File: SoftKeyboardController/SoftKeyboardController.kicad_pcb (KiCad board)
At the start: 2 copper layers, 175.9 x 135.9 mm, 44 parts, among them IC1 PCA9956BTWY, J1 Barrel_Jack, J2 Conn_01x08_Socket, J3 Motor 1, J4 Motor 2, J5 Conn_01x12_Socket, J6 Conn_01x12_Socket, J7 EXT IMU Connection, J8 Conn_01x08_Socket, Q1 Q_NMOS_GDS, Q10 Q_NMOS_GDS, Q11 Q_NMOS_GDS, Q12 Q_NMOS_GDS, Q13 Q_NMOS_GDS, Q14 Q_NMOS_GDS, Q15 Q_NMOS_GDS, Q16 Q_NMOS_GDS, Q2 Q_NMOS_GDS, Q3 Q_NMOS_GDS, Q4 Q_NMOS_GDS, Q5 Q_NMOS_GDS, Q6 Q_NMOS_GDS, Q7 Q_NMOS_GDS, Q8 Q_NMOS_GDS, Q9 Q_NMOS_GDS, U1 Motor Driver DRV8847PWR, U2 ADC128D818, U3 ADC128D818, U4 PI4IOE5V9539LEX

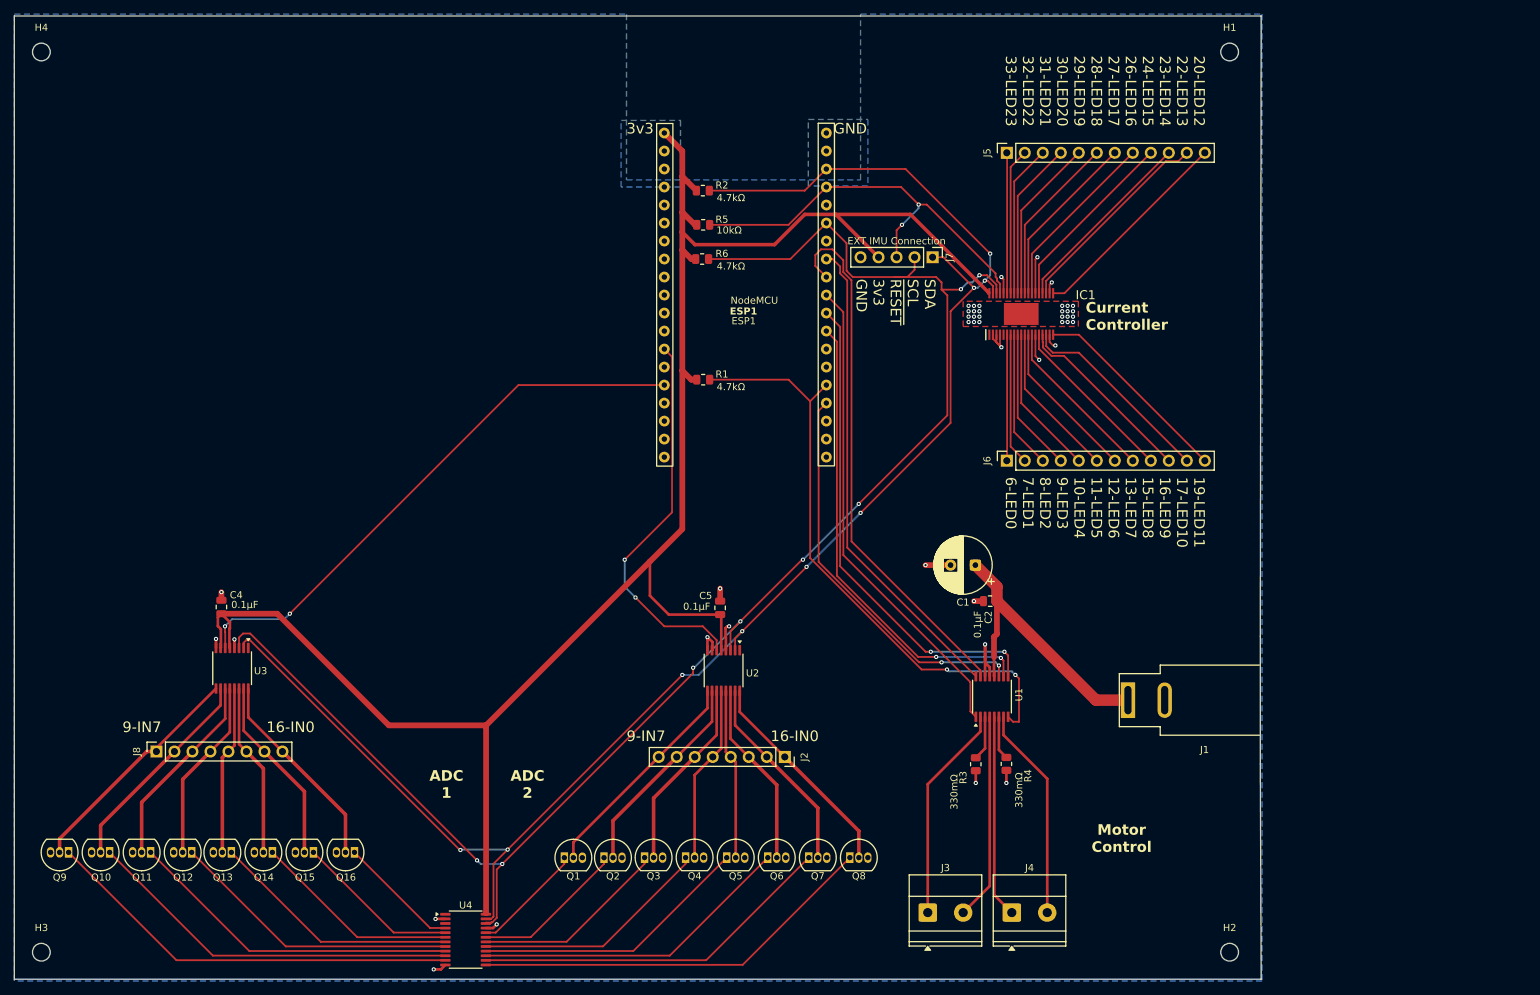
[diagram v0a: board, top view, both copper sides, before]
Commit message: Shrink Footprint
Relocated and re-traced board to improve overall footprint
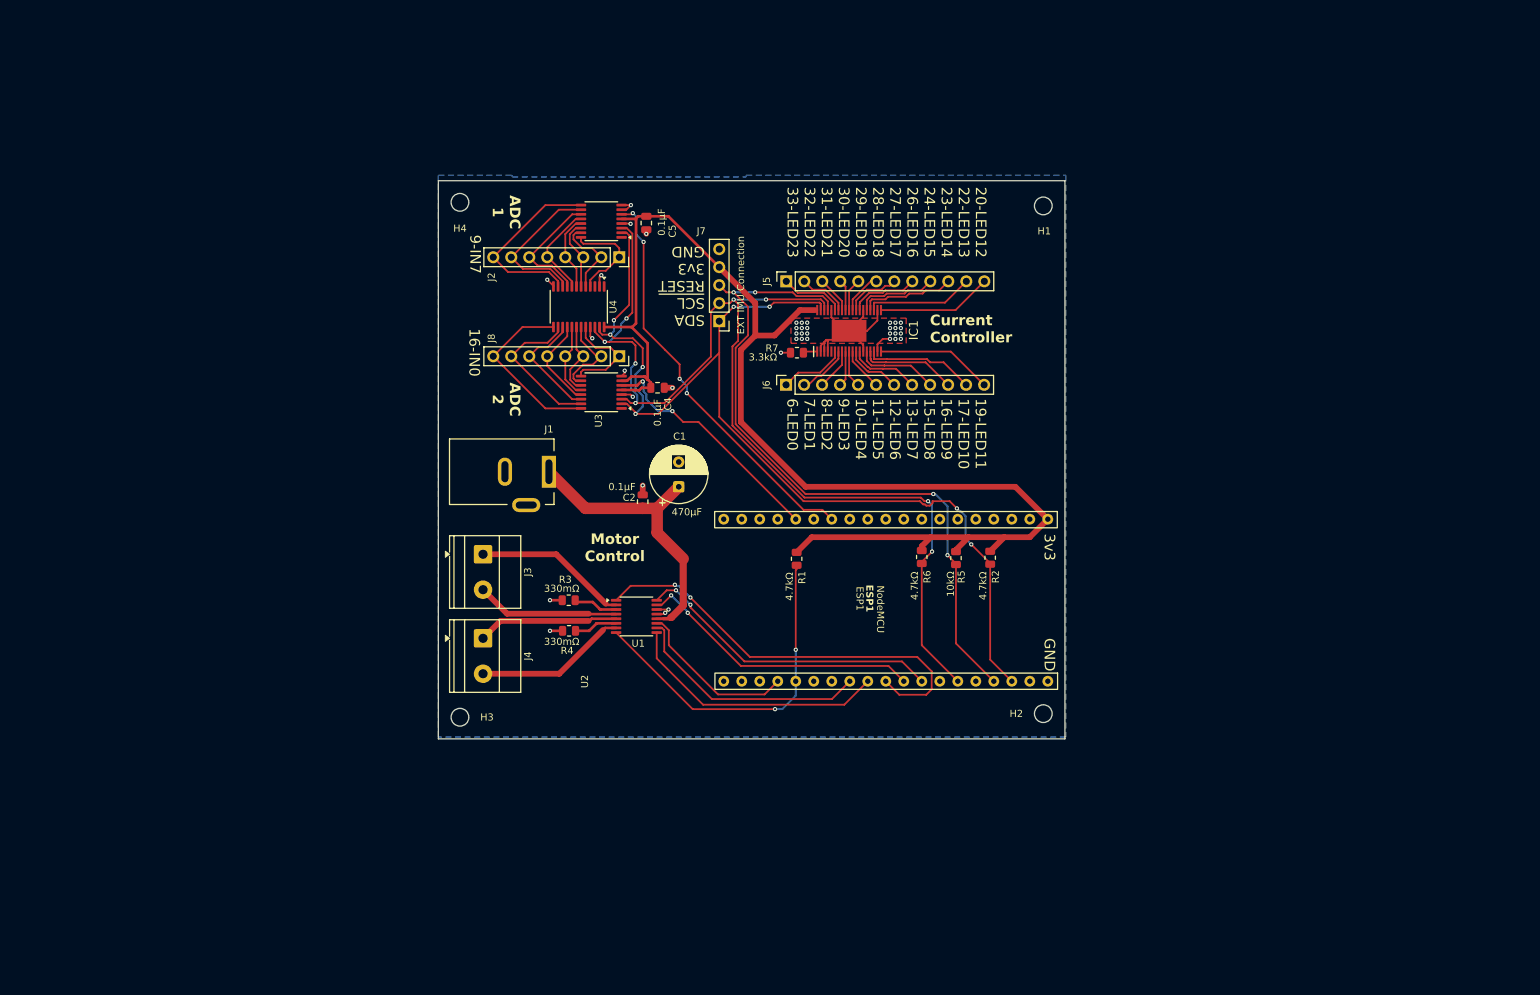
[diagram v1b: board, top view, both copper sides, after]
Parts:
- removed Q1, Q10, Q11, Q12, Q13, Q14, Q15, Q16, Q2, Q3, Q4, Q5, Q6, Q7, Q8, Q9: Q_NMOS_GDS, Package_TO_SOT_THT:TO-92_Inline
- added R7: 3.3kΩ, Resistor_SMD:R_0805_2012Metric, F.Cu at (139.6, 72.9)
- J1: footprint Connector_BarrelJack:BarrelJack_SwitchcraftConxall_RAPC10U_Horizontal -> Connector_BarrelJack:BarrelJack_Kycon_KLDX-0202-xC_Horizontal
- moved U4 90.7 mm to (108.8, 66.4), turned to -90 degrees
- moved J1 87.8 mm to (104.6, 89.7), turned to 0 degrees
- moved J8 85.9 mm to (114.6, 73.4), turned to -90 degrees
- moved J4 84.0 mm to (95.3, 113.2), turned to -90 degrees
- moved J3 80.6 mm to (95.3, 101.3), turned to -90 degrees
- moved J2 74.3 mm to (114.6, 59.4)
- moved C4 68.9 mm to (119.9, 77.9), turned to 0 degrees
- moved H3 67.7 mm to (92.1, 124.3)
- moved R2 65.8 mm to (166.9, 101.8), turned to -90 degrees
- moved U2 65.7 mm to (112.0, 54.4), turned to 180 degrees
- moved U3 65.0 mm to (112.0, 78.5), turned to 180 degrees
- moved R4 64.5 mm to (107.5, 112.1), turned to 0 degrees
- moved H4 62.7 mm to (92.1, 51.7)
- moved R3 61.9 mm to (107.4, 107.8), turned to 0 degrees
- moved R5 59.0 mm to (162.1, 101.9), turned to -90 degrees
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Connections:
- IC1 pad 1: unconnected-(IC1-REXT-Pad1) -> Net-(IC1-REXT)
- U4 pad 10: Net-(Q10-G) -> Net-(J2-Pin_7)
- U4 pad 11: Net-(Q9-G) -> Net-(J2-Pin_8)
- U4 pad 13: Net-(Q8-G) -> Net-(J8-Pin_8)
- U4 pad 14: Net-(Q7-G) -> Net-(J8-Pin_7)
- U4 pad 15: Net-(Q6-G) -> Net-(J8-Pin_6)
- U4 pad 16: Net-(Q5-G) -> Net-(J8-Pin_5)
- U4 pad 17: Net-(Q4-G) -> Net-(J8-Pin_4)
- U4 pad 18: Net-(Q3-G) -> Net-(J8-Pin_3)
- U4 pad 19: Net-(Q2-G) -> Net-(J8-Pin_2)
- U4 pad 20: Net-(Q1-G) -> Net-(J8-Pin_1)
- U4 pad 4: Net-(Q16-G) -> Net-(J2-Pin_1)
- U4 pad 5: Net-(Q15-G) -> Net-(J2-Pin_2)
- U4 pad 6: Net-(Q14-G) -> Net-(J2-Pin_3)
- U4 pad 7: Net-(Q13-G) -> Net-(J2-Pin_4)
- U4 pad 8: Net-(Q12-G) -> Net-(J2-Pin_5)
- U4 pad 9: Net-(Q11-G) -> Net-(J2-Pin_6)
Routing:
- net SDA: track 235.0 -> 149.9 mm, vias 9 -> 8
- net +3V3: track 267.5 -> 184.2 mm
- net SCL: track 231.4 -> 154.0 mm
- net Net-(Q9-G): track 59.1 -> 0.00 mm
- net Net-(Q8-G): track 58.0 -> 0.00 mm
- net Net-(Q10-G): track 53.0 -> 0.00 mm
- net Net-(Q7-G): track 51.9 -> 0.00 mm
- net Net-(Q11-G): track 47.0 -> 0.00 mm
- net Net-(Q6-G): track 45.9 -> 0.00 mm
- net Net-(ESP1-GPIO13): track 79.1 -> 34.0 mm
- net Net-(Q12-G): track 40.9 -> 0.00 mm
- net Net-(ESP1-GPIO1/TX0): track 59.4 -> 99.6 mm, vias 2 -> 4
- net Net-(Q5-G): track 39.8 -> 0.00 mm
- net Net-(ESP1-GPIO2): track 85.2 -> 49.1 mm
- net Net-(Q13-G): track 35.0 -> 0.00 mm
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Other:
- board size 175.9 x 135.9 mm -> 88.4 x 78.7 mm

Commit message: Remapped Board again
Version of Board before ordering
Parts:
- removed U1: Motor Driver DRV8847PWR, Package_SO:TSSOP-16_4.4x5mm_P0.65mm
- added C3: 10μF, Capacitor_SMD:C_0805_2012Metric, F.Cu at (170.1, 93.3)
- added C6: 2.2μF, Capacitor_SMD:C_0805_2012Metric, F.Cu at (181.1, 98.9)
- added J10: Motor Encoder 1, Connector_Molex:Molex_KK-396_A-41792-0005_1x05_P3.96mm_Horizontal, F.Cu at (161.9, 68.3)
- added J9: Motor Encoder 2, Connector_Molex:Molex_KK-396_A-41792-0005_1x05_P3.96mm_Horizontal, F.Cu at (161.9, 90.5)
- added R10: 470Ω, Resistor_SMD:R_0805_2012Metric, F.Cu at (165.9, 77.8)
- added R11: 470Ω, Resistor_SMD:R_0805_2012Metric, F.Cu at (165.9, 83.4)
- added R12: 100, Resistor_SMD:R_0805_2012Metric, F.Cu at (188.6, 72.2)
- added R13: 10kΩ, Resistor_SMD:R_0805_2012Metric, F.Cu at (183.0, 76.6)
- added R14: 1kΩ, Resistor_SMD:R_0805_2012Metric, F.Cu at (183.9, 69.6)
- added R8: 470Ω, Resistor_SMD:R_0805_2012Metric, F.Cu at (166.1, 62.1)
- added R9: 470Ω, Resistor_SMD:R_0805_2012Metric, F.Cu at (166.1, 54.4)
- added TP1: TestPoint, TestPoint:TestPoint_Loop_D1.80mm_Drill1.0mm_Beaded, F.Cu at (187.5, 76.5)
- added TP10: TestPoint, TestPoint:TestPoint_Loop_D1.80mm_Drill1.0mm_Beaded, F.Cu at (177.3, 76.8)
- added TP11: TestPoint, TestPoint:TestPoint_Loop_D1.80mm_Drill1.0mm_Beaded, F.Cu at (170.4, 97.6)
- added TP2: TestPoint, TestPoint:TestPoint_Loop_D1.80mm_Drill1.0mm_Beaded, F.Cu at (191.1, 76.4)
- added TP3: TestPoint, TestPoint:TestPoint_Loop_D1.80mm_Drill1.0mm_Beaded, F.Cu at (227.1, 114.1)
- added TP4: TestPoint, TestPoint:TestPoint_Loop_D1.80mm_Drill1.0mm_Beaded, F.Cu at (219.7, 113.8)
- added TP5: TestPoint, TestPoint:TestPoint_Loop_D1.80mm_Drill1.0mm_Beaded, F.Cu at (204.1, 67.9)
- added TP6: TestPoint, TestPoint:TestPoint_Loop_D1.80mm_Drill1.0mm_Beaded, F.Cu at (202.9, 72.6)
- added TP7: TestPoint, TestPoint:TestPoint_Loop_D1.80mm_Drill1.0mm_Beaded, F.Cu at (179.5, 47.7)
- added TP8: TestPoint, TestPoint:TestPoint_Loop_D1.80mm_Drill1.0mm_Beaded, F.Cu at (175.3, 48.8)
- added TP9: TestPoint, TestPoint:TestPoint_Loop_D1.80mm_Drill1.0mm_Beaded, F.Cu at (167.6, 88.4)
- added U5: CD74HC4067SM, Package_SO:SSOP-24_5.3x8.2mm_P0.65mm, F.Cu at (185.2, 63.6)
- added U6: DRV8848, Package_SO:TSSOP-16-1EP_4.4x5mm_P0.65mm, F.Cu at (175.2, 101.2)
- J1: value Barrel_Jack -> Barrel_Jack_Switch; footprint Connector_BarrelJack:BarrelJack_Kycon_KLDX-0202-xC_Horizontal -> Connector_BarrelJack:BarrelJack_CUI_PJ-102AH_Horizontal
- R1: value 4.7kΩ -> 10kΩ
- R3, R4: value 330mΩ -> 500mΩ
- U4: value PI4IOE5V9539LEX -> TL071; footprint Package_SO:TSSOP-24_4.4x7.8mm_P0.65mm -> Package_TO_SOT_SMD:SOT-23-5
- moved H4 144.2 mm to (236.2, 47.0)
- moved H3 101.3 mm to (157.5, 47.0)
- moved H1 89.5 mm to (236.2, 116.8)
- moved U2 87.6 mm to (198.2, 70.1), turned to 90 degrees
- moved J4 83.1 mm to (178.3, 116.4), turned to 0 degrees
- moved C5 80.6 mm to (195.7, 77.4)
- moved J7 79.6 mm to (193.1, 72.6), turned to 180 degrees
- moved J2 77.3 mm to (204.5, 53.6), turned to 0 degrees
- moved U4 75.6 mm to (184.2, 72.7), turned to 180 degrees
- moved J3 72.7 mm to (166.5, 116.4), turned to 0 degrees
- moved R7 72.3 mm to (211.9, 71.4)
- moved IC1 72.1 mm to (219.0, 66.7)
- moved J6 72.1 mm to (210.1, 74.3)
- moved J5 72.1 mm to (210.1, 59.7)
- moved R4 69.7 mm to (177.0, 108.5), turned to 90 degrees
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- renumbered J7 to J2, J2 to J7
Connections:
- ESP1 pad 10: unconnected-(ESP1-GPIO26/DAC2-Pad10) -> s0
- ESP1 pad 11: unconnected-(ESP1-GPIO27-Pad11) -> Net-(ESP1-GPIO27)
- ESP1 pad 12: unconnected-(ESP1-GPIO14-Pad12) -> Net-(ESP1-GPIO14)
- ESP1 pad 19: unconnected-(ESP1-Vin5V-Pad19) -> 5v
- ESP1 pad 23: Net-(ESP1-GPIO15) -> unconnected-(ESP1-GPIO15-Pad23)
- ESP1 pad 26: unconnected-(ESP1-GPIO4-Pad26) -> Net-(ESP1-GPIO4)
- ESP1 pad 29: Net-(ESP1-GPIO5) -> unconnected-(ESP1-GPIO5-Pad29)
- ESP1 pad 3: unconnected-(ESP1-GPIO36/ADC0-Pad3) -> I_Op
- ESP1 pad 4: unconnected-(ESP1-GPI39/ADC3-Pad4) -> Net-(ESP1-GPI39/ADC3)
- ESP1 pad 5: unconnected-(ESP1-GPI34/ADC6-Pad5) -> Net-(ESP1-GPI34/ADC6)
- ESP1 pad 6: unconnected-(ESP1-GPI35/ADC7-Pad6) -> ~{Multi}
- ESP1 pad 7: unconnected-(ESP1-GPIO32/ADC4-Pad7) -> s3
- ESP1 pad 8: unconnected-(ESP1-GPIO33/ADC5-Pad8) -> s2
- ESP1 pad 9: unconnected-(ESP1-GPIO25/DAC1-Pad9) -> s1
- J1 pad 3: (no net) -> unconnected-(J1-Pad3)
- J2 pad 1: SDA -> Net-(ESP1-GPIO1/TX0)
- J2 pad 3: Net-(ESP1-GPIO1/TX0) -> SDA
- J7 pad 1: Net-(J2-Pin_1) -> Net-(J7-Pin_1)
- J7 pad 2: Net-(J2-Pin_2) -> Net-(J7-Pin_2)
- J7 pad 3: Net-(J2-Pin_3) -> Net-(J7-Pin_3)
- J7 pad 4: Net-(J2-Pin_4) -> Net-(J7-Pin_4)
- J7 pad 5: Net-(J2-Pin_5) -> Net-(J7-Pin_5)
- J7 pad 6: Net-(J2-Pin_6) -> Net-(J7-Pin_6)
- J7 pad 7: Net-(J2-Pin_7) -> Net-(J7-Pin_7)
- J7 pad 8: Net-(J2-Pin_8) -> Net-(J7-Pin_8)
- R1 pad 2: Net-(ESP1-GPIO2) -> Net-(ESP1-GPIO4)
- U2 pad 10: Net-(J2-Pin_7) -> Net-(J7-Pin_7)
- U2 pad 11: Net-(J2-Pin_6) -> Net-(J7-Pin_6)
- U2 pad 12: Net-(J2-Pin_5) -> Net-(J7-Pin_5)
- U2 pad 13: Net-(J2-Pin_4) -> Net-(J7-Pin_4)
- U2 pad 14: Net-(J2-Pin_3) -> Net-(J7-Pin_3)
- U2 pad 15: Net-(J2-Pin_2) -> Net-(J7-Pin_2)
- U2 pad 16: Net-(J2-Pin_1) -> Net-(J7-Pin_1)
- U2 pad 6: Net-(ESP1-GPIO12) -> Net-(ESP1-GPI39/ADC3)
- U2 pad 9: Net-(J2-Pin_8) -> Net-(J7-Pin_8)
- U3 pad 6: Net-(ESP1-GPIO13) -> Net-(ESP1-GPI34/ADC6)
- U4 pad 1: unconnected-(U4-~{INT}-Pad1) -> I_Op
- U4 pad 3: unconnected-(U4-~{RESET}-Pad3) -> Net-(U4-+)
- U4 pad 4: Net-(J2-Pin_1) -> Net-(U4--)
- U4 pad 5: Net-(J2-Pin_2) -> +3V3
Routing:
- net s1: track 0.00 -> 139.4 mm
- net s0: track 0.00 -> 135.3 mm
- net ~{Multi}: track 0.00 -> 98.4 mm
- net s2: track 0.00 -> 98.0 mm
- net s3: track 0.00 -> 95.7 mm
- net 5v: track 0.00 -> 78.9 mm
- net Net-(ESP1-GPIO27): track 0.00 -> 70.2 mm
- net Net-(ESP1-GPIO5): track 60.6 -> 0.00 mm, vias 2 -> 0
- net Net-(ESP1-GPIO14): track 0.00 -> 59.8 mm
- net I_Op: track 0.00 -> 59.4 mm, vias 0 -> 2
- net Net-(ESP1-GPI34/ADC6): track 0.00 -> 59.4 mm, vias 0 -> 2
- net Net-(ESP1-GPIO4): track 0.00 -> 48.1 mm, vias 0 -> 2
- net Net-(ESP1-GPI39/ADC3): track 0.00 -> 37.3 mm, vias 0 -> 2
- net Net-(J2-Pin_8): track 26.7 -> 0.00 mm
- net Net-(J7-Pin_8): track 0.00 -> 25.5 mm
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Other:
- board size 88.4 x 78.7 mm -> 87.1 x 78.7 mm
- board text added: "ADC 1+2"
- board text added: "LED11 LED10 LED09 LED08 LED07 LED06 LED05 LED04 LED03 LED02 LED01 LED00"
- board text added: "LED12 LED13 LED14 LED15 LED16 LED17 LED18 LED19 LED20 LED21 LED22 LED23"
- board text added: "\(O.O)/"
- board text added: "~{RESET} SCL SDA 3v3 GND"
- board text removed: "19-LED11 17-LED10 16-LED9 15-LED8 13-LED7 12-LED6 11-LED5 10-LED4 9-LED3 8-LED2 7-LED1 6-LED0"
- board text removed: "20-LED12 22-LED13 23-LED14 24-LED15 26-LED16 27-LED17 28-LED18 29-LED19 30-LED20 31-LED21 32-LED22 33-LED23"
- board text removed: "ADC 1"
- board text removed: "ADC 2"
- board text removed: "SDA SCL ~{RESET} 3v3 GND"

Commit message: changed capacitor footprint to reflect actual capacitor
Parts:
- C1: footprint Capacitor_THT:CP_Radial_D8.0mm_P3.50mm -> Capacitor_THT:CP_Radial_D10.0mm_P5.00mm
- moved C6 1.76 mm to (182.2, 100.2)
- moved C1 1.68 mm to (177.2, 91.2)
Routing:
- net Net-(U6-VINT): track 8.99 -> 10.8 mm
- net Net-(U6-VM): track 23.5 -> 24.0 mm
